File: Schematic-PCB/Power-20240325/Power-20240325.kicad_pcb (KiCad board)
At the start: 2 copper layers, 53.9 x 82.9 mm, 37 parts, among them J2 Conn_01x05_Pin, SW2 Locker-SW, U1 PIC12F683-IMC

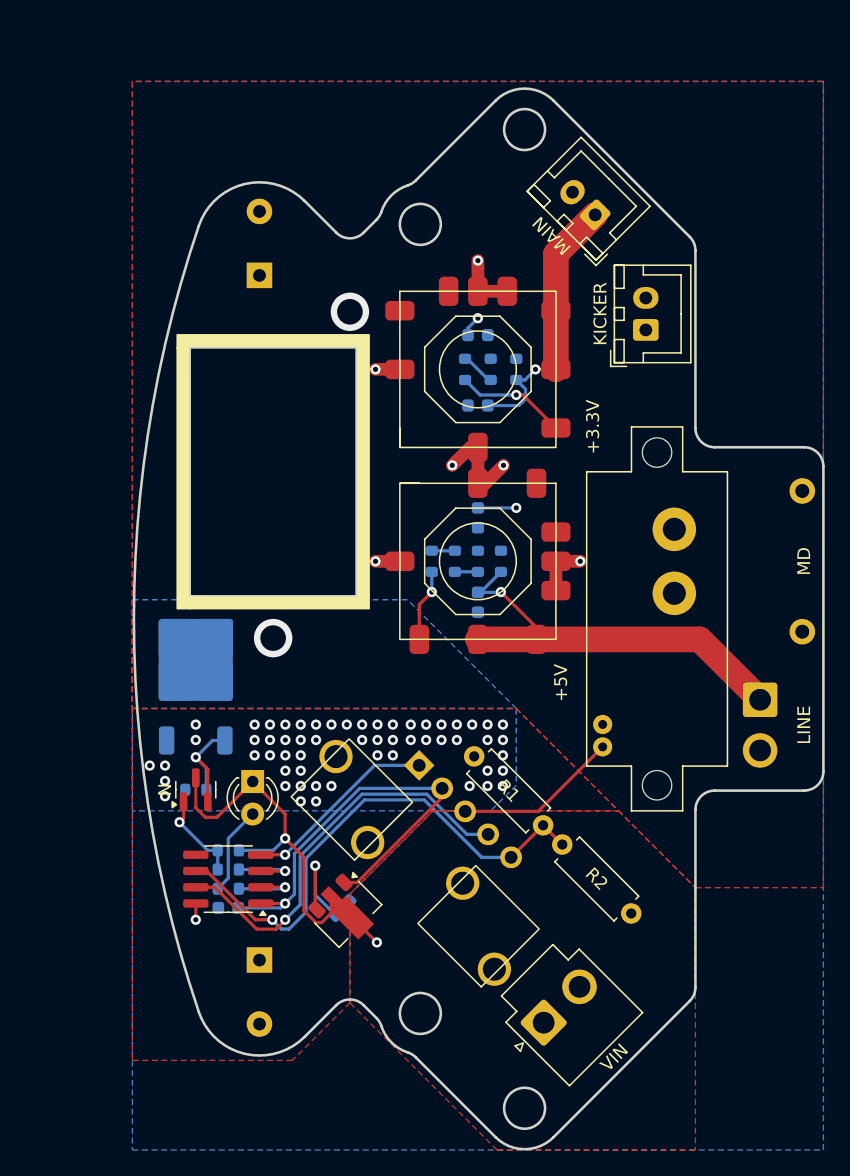
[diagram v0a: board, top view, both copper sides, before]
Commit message: キッカー基板 回路図の更新
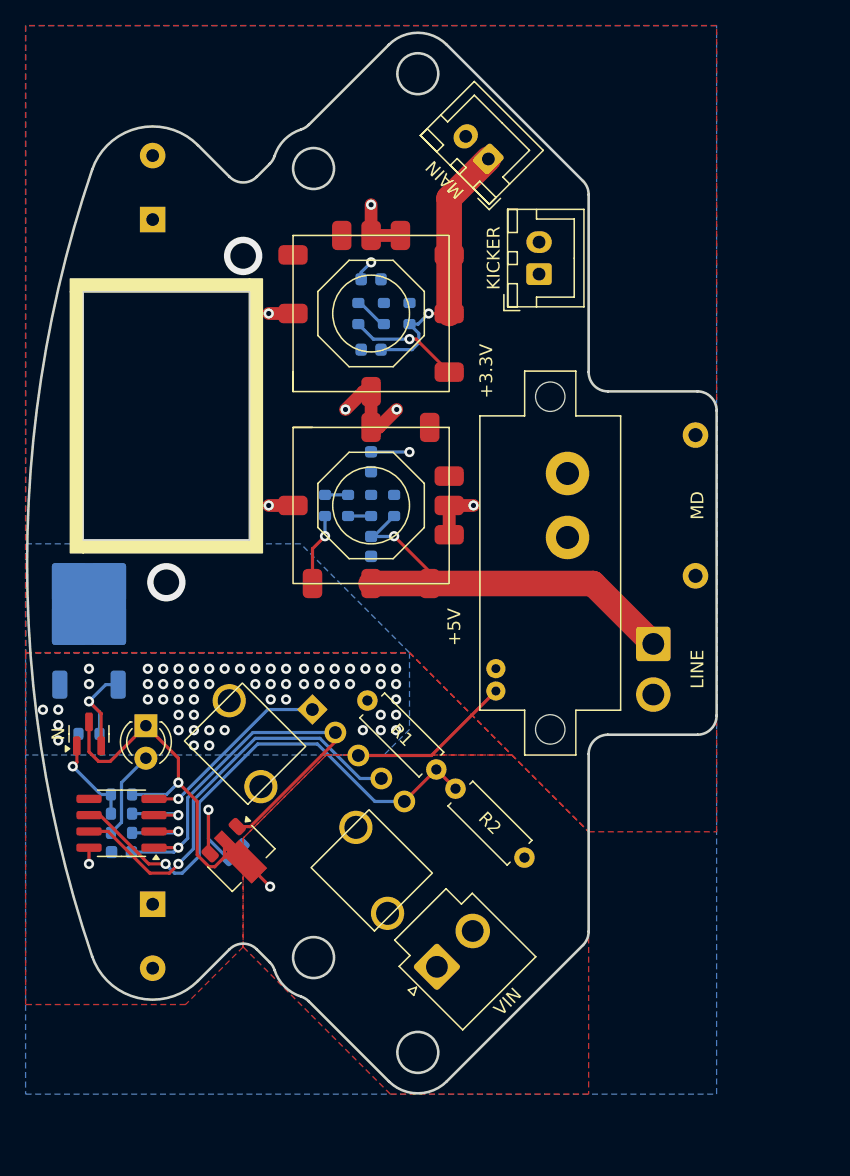
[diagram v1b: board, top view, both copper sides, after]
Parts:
- removed 1.2K, 1.5K: 1.2K, Resistor_SMD:R_0603_1608Metric
- removed 1.5K: 1.5K, Resistor_SMD:R_0603_1608Metric
- removed 10: 10, Resistor_SMD:R_0603_1608Metric
- removed 100: 100, Resistor_SMD:R_0603_1608Metric
- removed 10K (x2): 10K, Resistor_SMD:R_0603_1608Metric
- removed 10u, 22u (x2): 22uF, Capacitor_SMD:C_0603_1608Metric
- removed 10u: 10uF, Capacitor_SMD:C_0603_1608Metric
- removed 1K: 1K, Resistor_SMD:R_0603_1608Metric
- removed 1u: 1.0uF, Capacitor_SMD:C_0603_1608Metric
- removed 2.2u: 2.2uF, Capacitor_SMD:C_0603_1608Metric
- removed 330 (x2): 330, Resistor_SMD:R_0603_1608Metric
- removed 680: 680, Resistor_SMD:R_0603_1608Metric
- added C1: 22uF, Capacitor_SMD:C_0603_1608Metric, B.Cu at (89.5, 115.0)
- added C2: 10uF, Capacitor_SMD:C_0603_1608Metric, B.Cu at (89.5, 120.5)
- added C3: 1.0uF, Capacitor_SMD:C_0603_1608Metric, B.Cu at (78.9, 159.8)
- added C4: 22uF, Capacitor_SMD:C_0603_1608Metric, B.Cu at (89.5, 129.3)
- added C5: 2.2uF, Capacitor_SMD:C_0603_1608Metric, B.Cu at (70.0, 159.8)
- added C8: 10uF, Capacitor_SMD:C_0603_1608Metric, B.Cu at (89.5, 135.9)
- added R10: 100, Resistor_SMD:R_0603_1608Metric, B.Cu at (70.0, 156.8)
- added R12: 1K, Resistor_SMD:R_0603_1608Metric, B.Cu at (85.9, 132.7)
- added R13: 10, Resistor_SMD:R_0603_1608Metric, B.Cu at (89.5, 132.7)
- added R14: 330, Resistor_SMD:R_0603_1608Metric, B.Cu at (87.7, 132.7)
- added R15: 1.2K, Resistor_SMD:R_0603_1608Metric, B.Cu at (91.3, 132.7)
- added R4: 10K, Resistor_SMD:R_0603_1608Metric, B.Cu at (67.5, 150.5)
- added R5: 330, Resistor_SMD:R_0603_1608Metric, B.Cu at (70.0, 158.3)
- added R6: 1.5K, Resistor_SMD:R_0603_1608Metric, B.Cu at (88.5, 117.7)
- added R7: 680, Resistor_SMD:R_0603_1608Metric, B.Cu at (90.5, 117.7)
- added R8: 1.2K, Resistor_SMD:R_0603_1608Metric, B.Cu at (92.5, 117.7)
- added R9: 10K, Resistor_SMD:R_0603_1608Metric, B.Cu at (70.0, 155.3)
- moved R1 9.42 mm to (89.2, 147.9)
- moved R2 9.42 mm to (96.1, 154.8)
- moved +3.3V 9.42 mm to (89.5, 117.7)
- moved C6 9.42 mm to (72.4, 110.3)
- moved D1 9.42 mm to (71.9, 149.9)
- moved LINE 9.42 mm to (111.6, 143.5)
- moved P 9.42 mm to (67.5, 141.6)
- moved U1 9.42 mm to (70.0, 157.5)
- moved U3 9.42 mm to (79.4, 160.2)
- moved VIN 9.42 mm to (94.6, 168.7)
- moved KICKER 9.42 mm to (102.6, 114.6)
- moved MAIN 9.42 mm to (98.7, 105.6)
- moved SW2 9.42 mm to (73.5, 125.7)
- moved +5V 9.42 mm to (89.5, 132.7)
- moved C7 9.42 mm to (72.4, 163.8)
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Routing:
- net VIN: track 5.90 -> 4.06 mm, vias 3 -> 2
- net GND: track 67.9 -> 69.7 mm, vias 9 -> 10

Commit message: 電源基板の回路図/PCBデザインを更新しました。
メイン基板への供給ラインを増やしました。
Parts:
- removed MAIN: Conn_01x02_Pin, Connector_JST:JST_XH_B2B-XH-A_1x02_P2.50mm_Vertical
- added J5: Conn_01x03_Pin, Connector_JST:JST_XH_B3B-XH-A_1x03_P2.50mm_Vertical, F.Cu at (88.8, 112.6)
- moved KICKER 14.6 mm to (91.0, 123.3)
- moved C5 12.7 mm to (58.5, 165.1)
- moved D1 12.7 mm to (60.4, 155.2)
- moved R10 12.7 mm to (58.5, 162.1)
- moved R5 12.7 mm to (58.5, 163.6)
- moved R9 12.7 mm to (58.5, 160.6)
- moved U1 12.7 mm to (58.5, 162.8)
- moved +3.3V 12.7 mm to (78.0, 123.0)
- moved C1 12.7 mm to (78.0, 120.3), turned to 0 degrees
- moved C2 12.7 mm to (78.0, 125.8)
- moved C3 12.7 mm to (67.4, 165.1)
- moved C4 12.7 mm to (78.0, 134.6)
- moved C6 12.7 mm to (60.9, 115.7)
- moved C7 12.7 mm to (60.9, 169.2)
- moved C8 12.7 mm to (78.0, 141.2)
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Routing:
- net +5V: track 33.1 -> 75.5 mm
- net VIN: track 4.06 -> 5.90 mm, vias 2 -> 3
- net GND: track 69.7 -> 67.9 mm, vias 10 -> 9

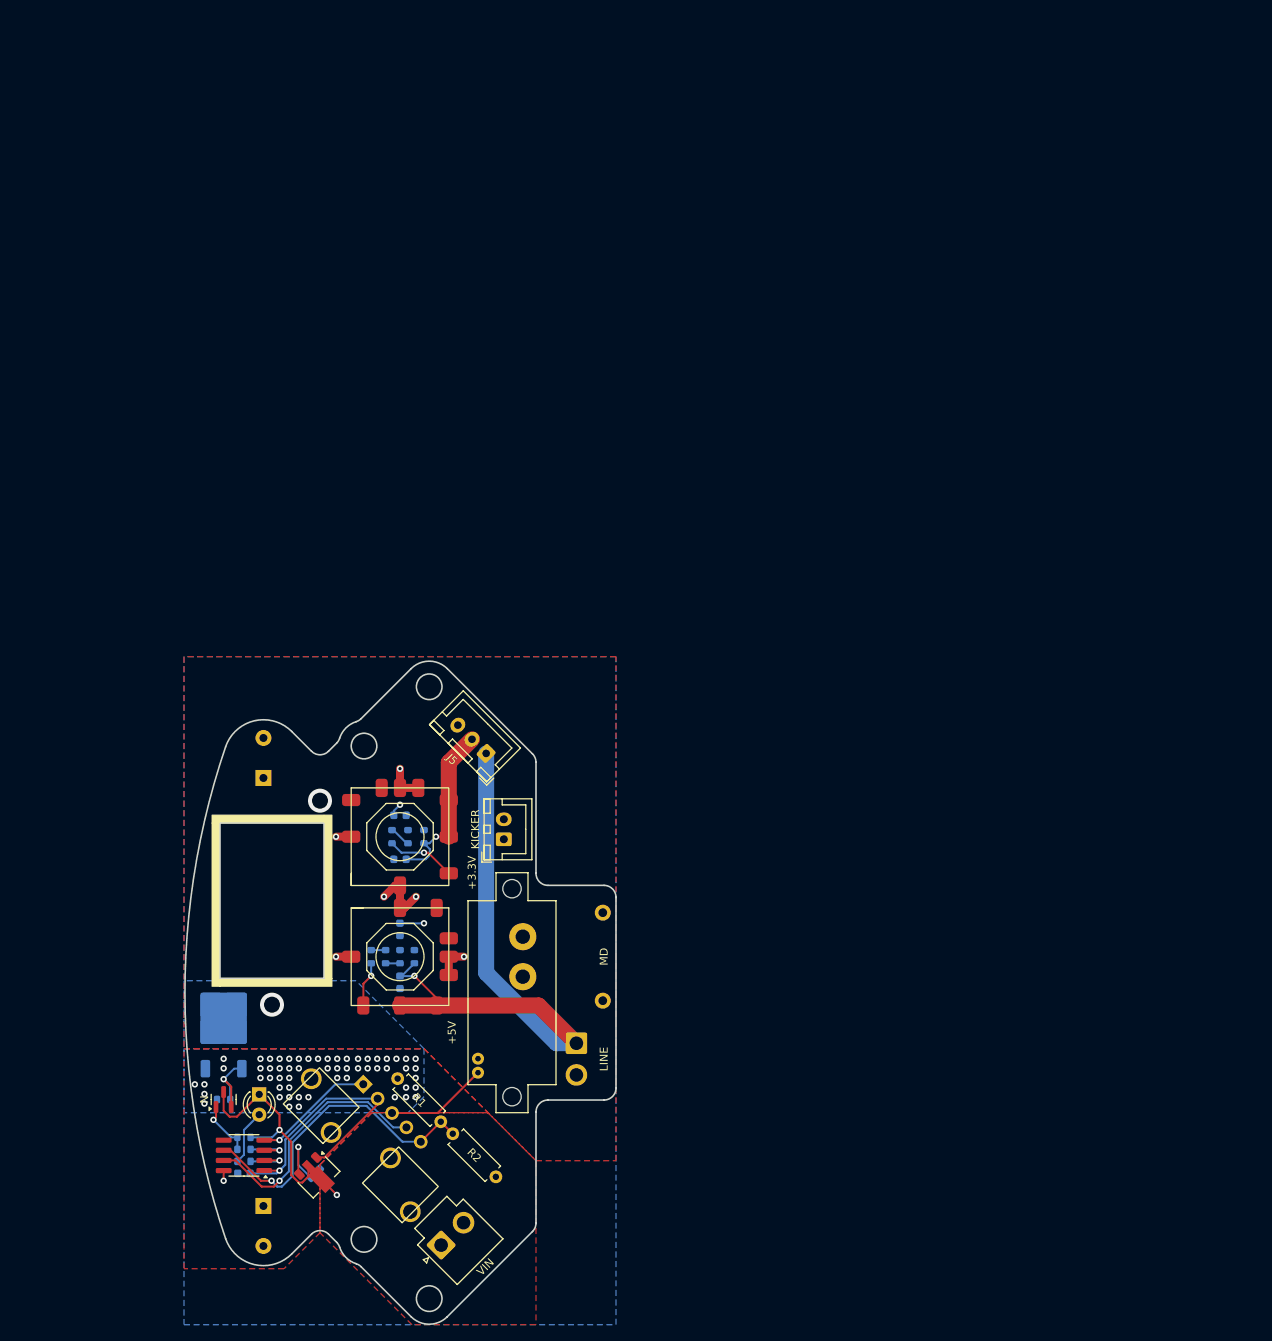
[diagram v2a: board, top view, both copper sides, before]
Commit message: 電源基板を更新
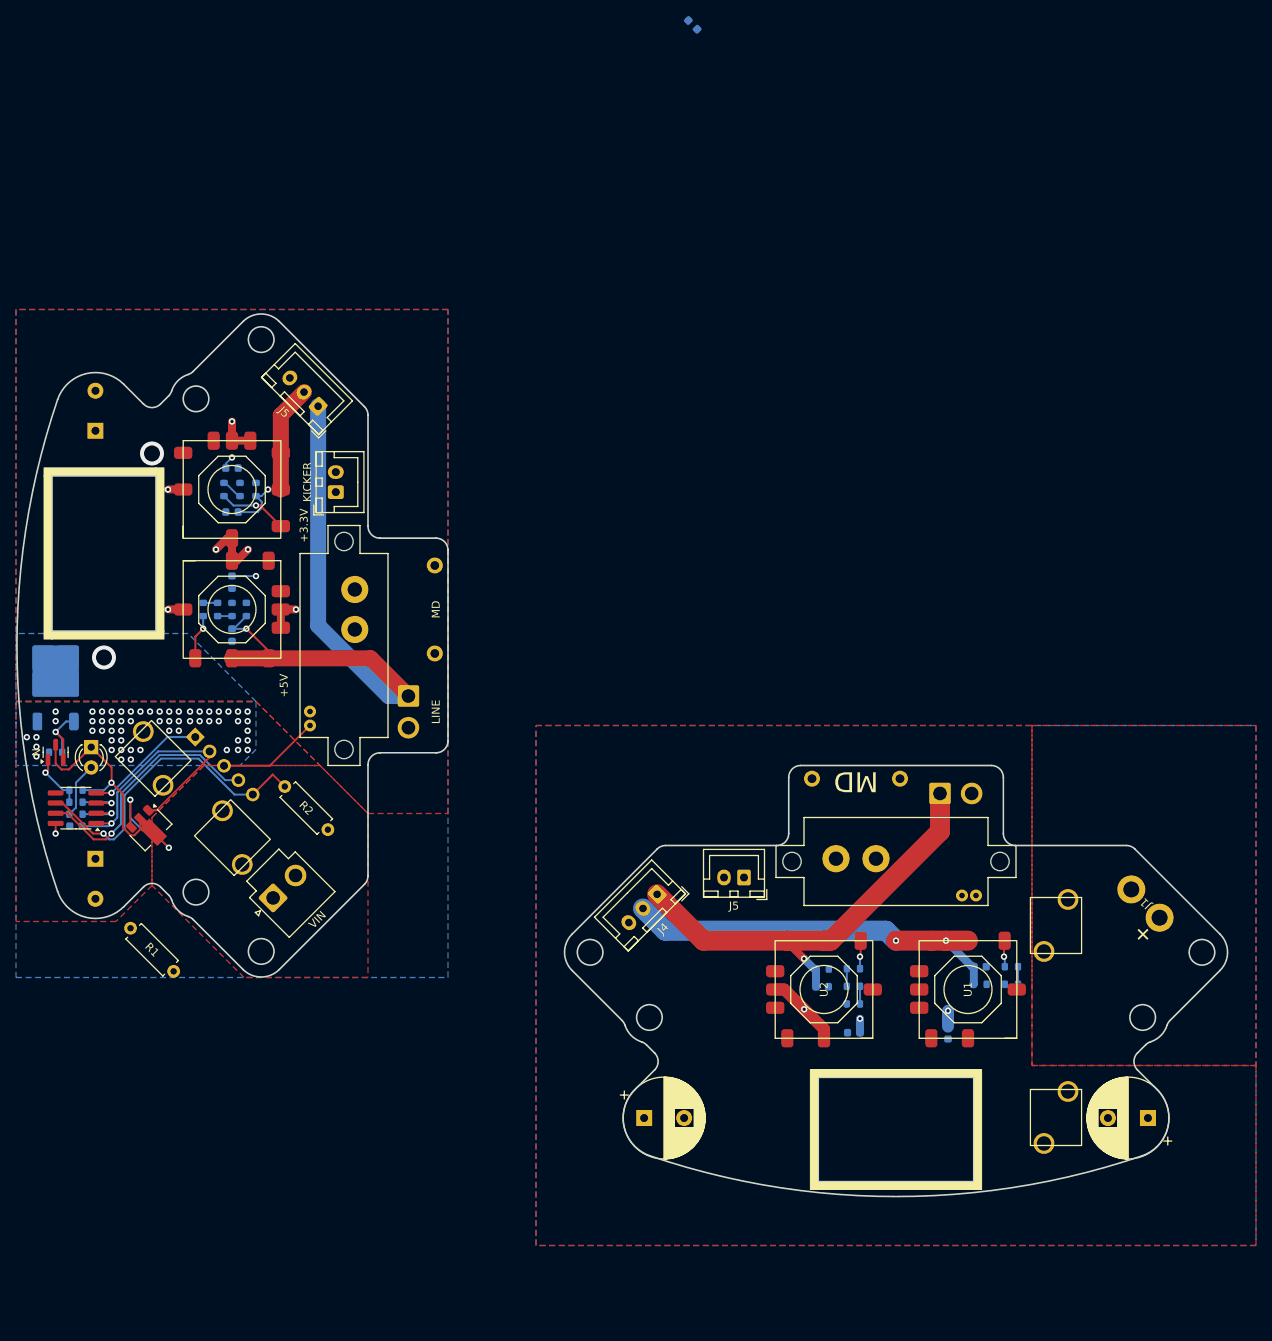
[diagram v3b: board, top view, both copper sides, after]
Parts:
- removed the C1 at (78.0, 120.3)
- removed the C2 at (78.0, 125.8)
- removed the C3 at (67.4, 165.1)
- removed the C4 at (78.0, 134.6)
- removed the C5 at (58.5, 165.1)
- removed the C6 at (60.9, 115.7)
- removed the F1 at (73.1, 161.6)
- removed the J5 at (88.8, 112.6)
- removed the MD at (93.3, 138.0)
- removed the R1 at (77.7, 153.2)
- removed the R2 at (84.6, 160.1)
- removed the R4 at (56.0, 155.8)
- removed the R5 at (58.5, 163.6)
- removed the R6 at (77.0, 123.0)
- removed the R7 at (79.0, 123.0)
- removed the U1 at (58.5, 162.8)
- added +: Voltmeter_DC, @2024-Power:VoltMeter, F.Cu at (140.0, 126.1)
- added C1: 22uF, Capacitor_SMD:C_0603_1608Metric, B.Cu at (146.5, 147.5)
- added C1: 22uF, Capacitor_SMD:C_0603_1608Metric, B.Cu at (57.0, 76.9)
- added C2: 10uF, Capacitor_SMD:C_0603_1608Metric, B.Cu at (150.5, 139.2)
- added C2: 10uF, Capacitor_SMD:C_0603_1608Metric, B.Cu at (57.0, 82.4)
- added C3: 1.0uF, Capacitor_SMD:C_0603_1608Metric, B.Cu at (114.6, 21.5)
- added C3: 22uF, Capacitor_SMD:C_0603_1608Metric, B.Cu at (134.7, 147.5)
- added C4: 1000uF, Capacitor_THT:CP_Radial_D10.0mm_P5.00mm, F.Cu at (171.5, 158.2)
- added C4: 22uF, Capacitor_SMD:C_0603_1608Metric, B.Cu at (57.0, 91.2)
- added C5: 1000uF, Capacitor_THT:CP_Radial_D10.0mm_P5.00mm, F.Cu at (108.5, 158.2)
- added C5: 2.2uF, Capacitor_SMD:C_0603_1608Metric, B.Cu at (37.5, 121.7)
- added C6: 1000uF, Capacitor_THT:CP_Radial_D10.0mm_P5.00mm, B.Cu at (39.9, 72.3)
- added C6: 10uF, Capacitor_SMD:C_0603_1608Metric, B.Cu at (130.8, 141.8)
- added F1: 10A/15A, @2024-Power:Fuse, F.Cu at (52.1, 118.2)
- added F1: 10A/15A, @2024-Power:Fuse, F.Cu at (160.0, 146.1)
- added J1: Conn_01x02_Pin, @2024-Power:VIN, F.Cu at (171.2, 131.4)
- added J3: Conn_01x02_Pin, Connector_JST:JST_VH_S2P-VH_1x02_P3.96mm_Horizontal, B.Cu at (145.5, 117.6)
- added J4: Conn_01x03_Pin, Connector_JST:JST_XH_B3B-XH-A_1x03_P2.50mm_Vertical, F.Cu at (110.1, 130.2)
- added J5: Conn_01x03_Pin, Connector_JST:JST_XH_B3B-XH-A_1x03_P2.50mm_Vertical, F.Cu at (67.8, 69.2)
- added J5: Conn_01x02_Pin, Connector_JST:JST_XH_B2B-XH-A_1x02_P2.50mm_Vertical, F.Cu at (121.0, 128.1)
- added MD: Conn_01x02_Pin, @2024-Power:XT30PW-M, B.Cu at (72.3, 94.6)
- added MD: Conn_01x02_Pin, @2024-Power:XT30PW-M, B.Cu at (135.0, 125.8)
- added R1: R, Resistor_THT:R_Axial_DIN0207_L6.3mm_D2.5mm_P7.62mm_Horizontal, F.Cu at (44.3, 134.4)
- added R1: 1.5K, Resistor_SMD:R_0603_1608Metric, B.Cu at (154.4, 139.2)
- added R2: R, Resistor_THT:R_Axial_DIN0207_L6.3mm_D2.5mm_P7.62mm_Horizontal, F.Cu at (63.6, 116.7)
- added R2: 680, Resistor_SMD:R_0603_1608Metric, B.Cu at (154.4, 141.4)
- added R3: 1.2K, Resistor_SMD:R_0603_1608Metric, B.Cu at (150.5, 141.4)
- added R4: 1K, Resistor_SMD:R_0603_1608Metric, B.Cu at (134.7, 139.5)
- added R4: 10K, Resistor_SMD:R_0603_1608Metric, B.Cu at (35.0, 112.5)
- added R5: 10, Resistor_SMD:R_0603_1608Metric, B.Cu at (134.7, 143.9)
- added R5: 330, Resistor_SMD:R_0603_1608Metric, B.Cu at (37.5, 120.2)
- added R6: 330, Resistor_SMD:R_0603_1608Metric, B.Cu at (134.7, 141.7)
- added R6: 1.5K, Resistor_SMD:R_0603_1608Metric, B.Cu at (56.0, 79.6)
- added R7: 1.2K, Resistor_SMD:R_0603_1608Metric, B.Cu at (130.8, 139.6)
- added R7: 680, Resistor_SMD:R_0603_1608Metric, B.Cu at (58.0, 79.6)
- added SW1: SW_DPST_x2, @2024-Power:RA1113112R, F.Cu at (140.0, 159.6)
- added U1: PIC12F683-IMC, Package_SO:SOP-8_3.76x4.96mm_P1.27mm, F.Cu at (37.5, 119.4)
- added U1: ~, @2024-Power:OKL-T6-W12N-C, F.Cu at (149.0, 142.1)
- added U2: ~, @2024-Power:OKL-T6-W12N-C, F.Cu at (131.0, 142.1)
- moved VIN 48.2 mm to (62.1, 130.7)
- moved +3.3V 48.2 mm to (57.0, 79.6)
- moved C7 48.2 mm to (39.9, 125.8)
- moved C8 48.2 mm to (57.0, 97.8)
- moved KICKER 48.2 mm to (70.0, 79.9)
- moved N 48.2 mm to (35.0, 112.5)
- moved R8 48.2 mm to (60.0, 79.6)
- moved U3 48.2 mm to (46.9, 122.1)
- moved R12 48.2 mm to (53.4, 94.6)
- moved +5V 48.2 mm to (57.0, 94.6)
- moved D1 48.2 mm to (39.4, 111.8)
- moved J2 48.2 mm to (52.4, 110.5)
- moved LINE 48.2 mm to (79.1, 105.4)
- moved MES1 48.2 mm to (71.0, 99.1)
- moved P 48.2 mm to (35.0, 103.6)
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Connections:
- +5V pad 6: Net-(U4-Trim) -> (no net)
- C7 pad 1: V_RAW -> (no net)
- D1 pad 2: Net-(D1-A) -> (no net)
- J2 pad 1: MCLR/VPP -> (no net)
- J2 pad 2: +3.3VA -> (no net)
- J2 pad 4: ICSPDAT -> (no net)
- J2 pad 5: ICSPCLK -> (no net)
- N pad 1: Net-(Q2-G) -> (no net)
- N pad 2: Net-(Q1-G) -> (no net)
- P pad 1: Net-(Q1-G) -> (no net)
- P pad 2: Net-(Q1-D) -> (no net)
- P pad 3: V_RAW -> (no net)
- R10 pad 1: Net-(Q2-G) -> (no net)
- R10 pad 2: V_Control -> (no net)
- R12 pad 1: Net-(U4-Trim) -> (no net)
- R12 pad 2: Net-(R12-Pad2) -> (no net)
- R13 pad 2: Net-(R13-Pad2) -> (no net)
- R14 pad 1: Net-(R12-Pad2) -> (no net)
- R14 pad 2: Net-(R13-Pad2) -> (no net)
- R9 pad 1: Net-(Q2-G) -> (no net)
- U3 pad 1: +3.3VA -> (no net)
- U3 pad 3: V_RAW -> (no net)
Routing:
- net (no net): track 0.00 -> 178.2 mm, vias 0 -> 68
- net +5V: track 75.5 -> 131.0 mm, vias 1 -> 2
- net +3.3V: track 21.8 -> 71.1 mm, vias 1 -> 3
- net ICSPCLK: track 40.7 -> 0.00 mm, vias 1 -> 0
- net +3.3VA: track 34.7 -> 0.00 mm, vias 1 -> 0
- net ICSPDAT: track 32.1 -> 0.00 mm, vias 1 -> 0
- net MCLR/VPP: track 15.3 -> 0.00 mm, vias 1 -> 0
- net Net-(Q1-G): track 9.58 -> 0.00 mm, vias 1 -> 0
- net GND: track 67.9 -> 77.2 mm, vias 9 -> 10
- net V_RAW: track 8.00 -> 0.00 mm, vias 58 -> 0
- net Net-(D1-A): track 7.61 -> 0.00 mm
- net Net-(Q2-G): track 7.13 -> 0.00 mm, vias 1 -> 0
- net Net-(U4-Trim): track 5.68 -> 0.00 mm, vias 1 -> 0
- net V_Control: track 5.57 -> 0.00 mm, vias 1 -> 0
- net Net-(U1-GP5): track 5.57 -> 0.00 mm, vias 1 -> 0
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- added copper zone on B.Cu, net (none)
- added copper zone on F.Cu, net (none)
- removed copper zone on B.Cu, net Net-(Q1-D)
- removed copper zone on B.Cu, net V_RAW
- removed copper zone on F.Cu, net V_RAW
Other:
- board size 53.9 x 82.9 mm -> 151.3 x 110.3 mm
